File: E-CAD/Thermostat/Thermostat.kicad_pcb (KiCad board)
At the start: 2 copper layers, 71 x 71 mm, 29 parts, among them IC3 CPC1972GSTR, J1 Screw_Terminal_01x04, J2 Conn_01x04_Female_Display, J3 Conn_01x04_Female_Prog, J4 Conn_01x07_Male, J5 Conn_01x02_Male, J6 Conn_01x03_Male, J7 Conn_01x03_Male_DHT, Q1 BC847, Q2 BC847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

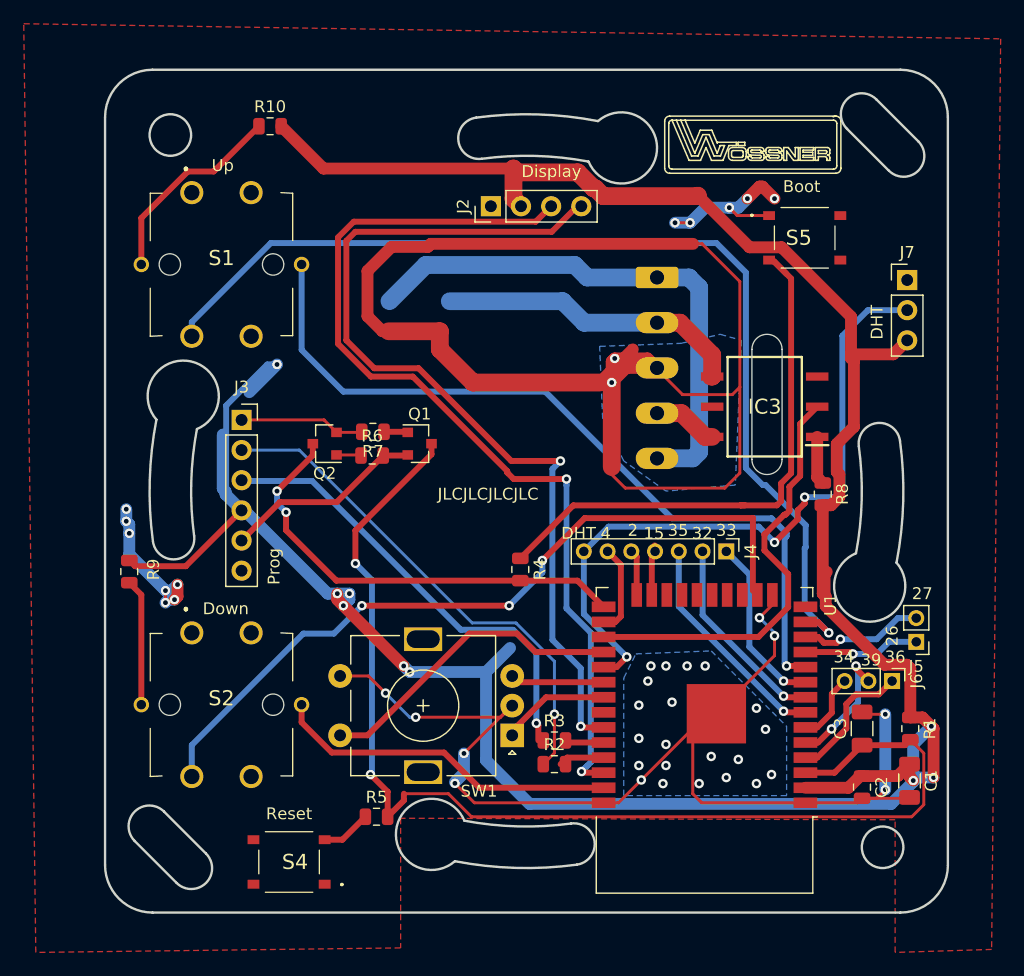
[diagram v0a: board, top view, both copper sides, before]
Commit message: adjusting to api v3 and home assistant
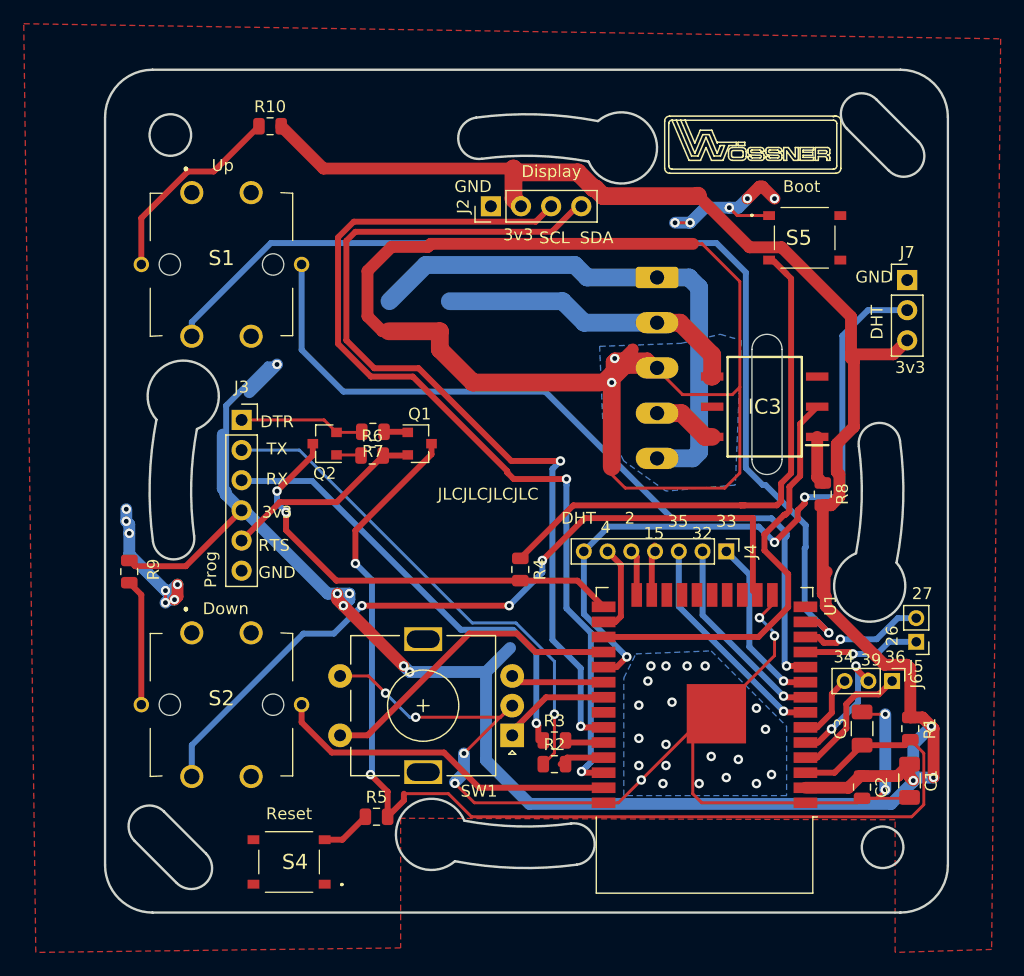
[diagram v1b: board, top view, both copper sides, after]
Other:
- board text added: "3v3"
- board text added: "DTR"
- board text added: "GND"
- board text added: "RTS"
- board text added: "RX"
- board text added: "SCL"
- board text added: "SDA"
- board text added: "TX"
